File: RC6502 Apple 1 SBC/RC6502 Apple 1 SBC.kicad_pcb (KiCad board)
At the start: 2 copper layers, 99.1 x 99.7 mm, 44 parts, among them J1 VP GND, J2 Arduino Nano, J3 Backplane, J4 Hole, J5 Hole, J6 Hole, J7 Hole, J8 Power, SW1 RESET, U1 WD65C02, U2 HM62256BLP-7, U3 74HCT138, U4 28C256, U5 74HCT00, U6 NE555, U7 74HCT04, U8 WD65C21, U9 MCP23S17, X1 1MHz

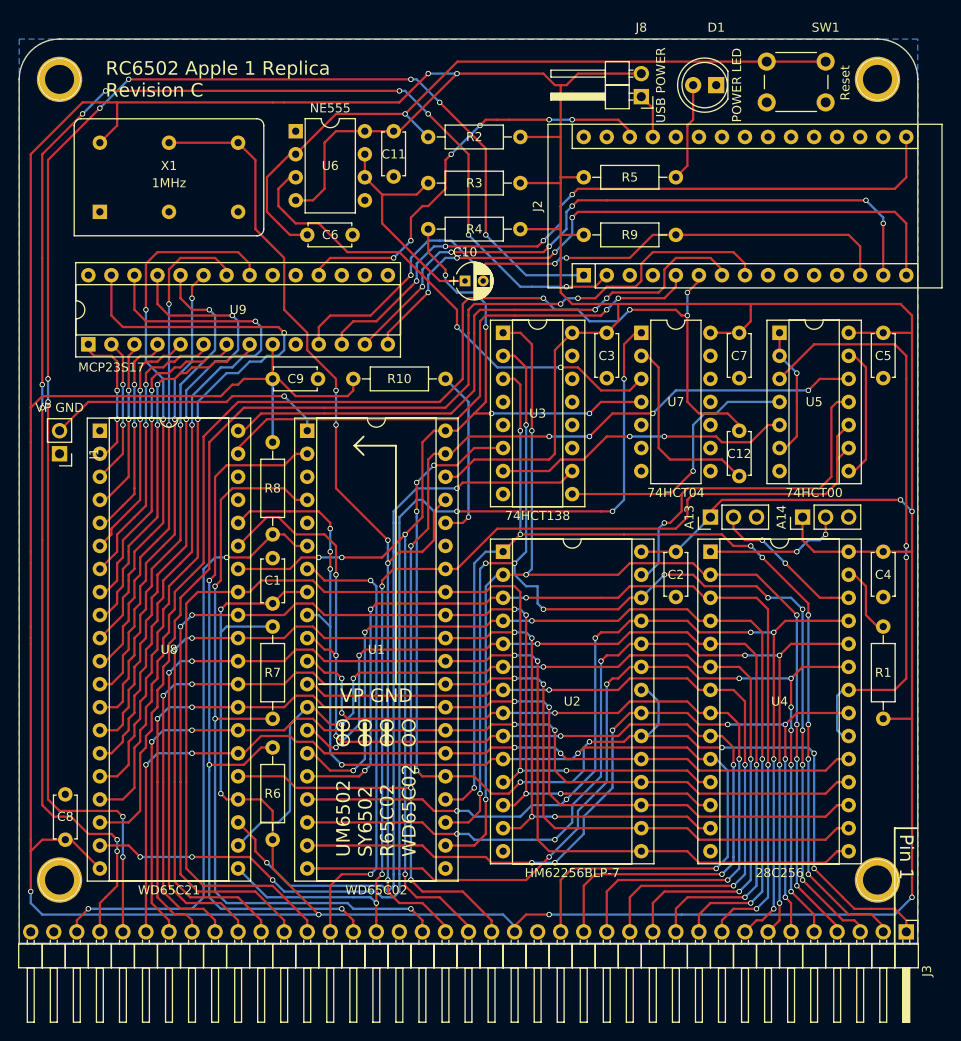
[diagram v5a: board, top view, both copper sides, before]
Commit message: Added resistor values to SBC silkscreen
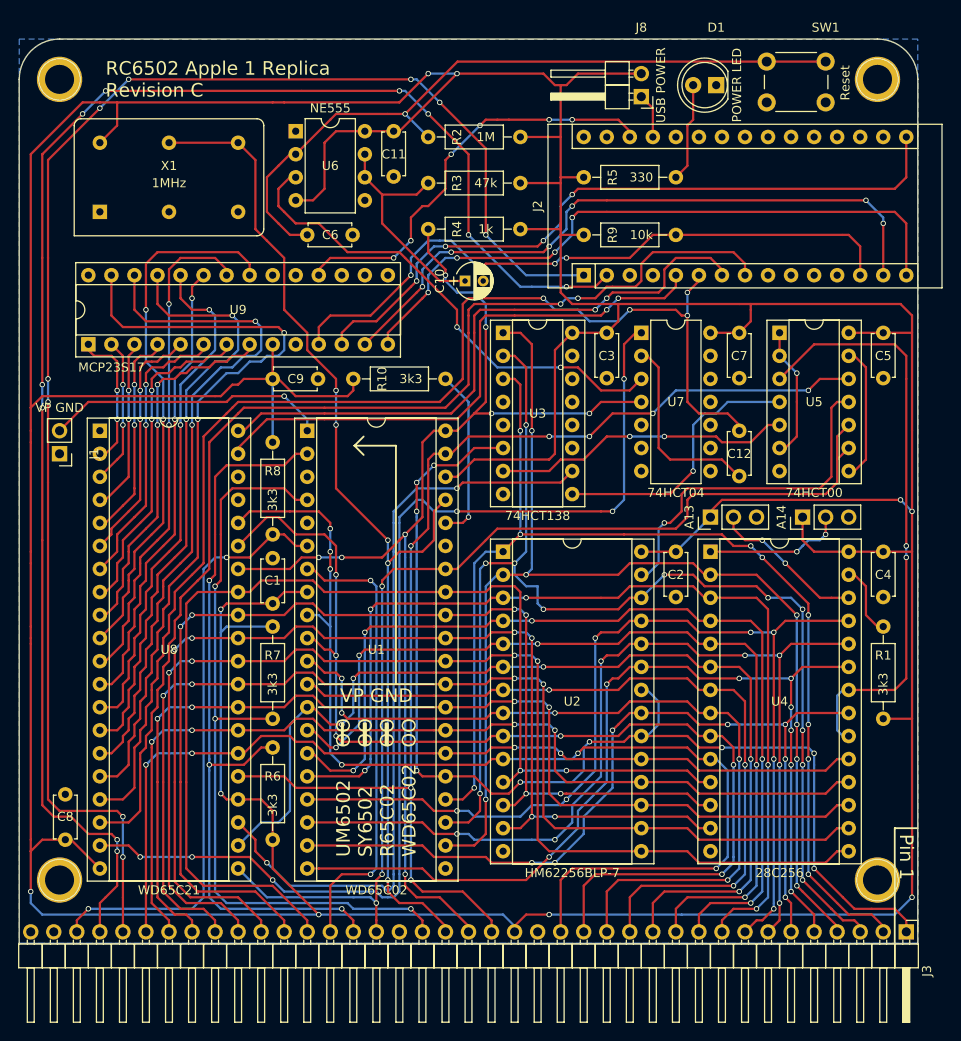
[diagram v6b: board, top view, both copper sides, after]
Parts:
- R1, R10, R6, R7, R8: value 3.3k -> 3k3
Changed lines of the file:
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@@
     (descr "Resistor, Axial_DIN0207 series, Axial, Horizontal, pin pitch=10.16mm, 0.25W = 1/4W, length*diameter=6.3*2.5mm^2, http://cdn-reichelt.de/documents/datenblatt/B400/1_4W%23YAG.pdf")
     (tags "Resistor Axial_DIN0207 series Axial Horizontal pin pitch 10.16mm 0.25W = 1/4W length 6.3mm diameter 2.5mm")
-    (fp_text reference R1 (at 5.08 0 360) (layer F.SilkS)
-      (effects (font (size 1 1) (thickness 0.15)))
-    )
-    (fp_text value 3.3k (at 5.715 -5.08 270) (layer F.Fab)
+    (fp_text reference R1 (at 3.175 0 360) (layer F.SilkS)
+      (effects (font (size 1 1) (thickness 0.15)))
+    )
+    (fp_text value 3k3 (at 6.35 0 270) (layer F.SilkS)
       (effects (font (size 1 1) (thickness 0.15)))
     )
@@
     (descr "Resistor, Axial_DIN0207 series, Axial, Horizontal, pin pitch=10.16mm, 0.25W = 1/4W, length*diameter=6.3*2.5mm^2, http://cdn-reichelt.de/documents/datenblatt/B400/1_4W%23YAG.pdf")
     (tags "Resistor Axial_DIN0207 series Axial Horizontal pin pitch 10.16mm 0.25W = 1/4W length 6.3mm diameter 2.5mm")
-    (fp_text reference R2 (at 5.08 0 180) (layer F.SilkS)
-      (effects (font (size 1 1) (thickness 0.15)))
-    )
-    (fp_text value 1M (at 5.08 1.905 180) (layer F.Fab)
+    (fp_text reference R2 (at 6.985 0 270) (layer F.SilkS)
+      (effects (font (size 1 1) (thickness 0.15)))
+    )
+    (fp_text value 1M (at 3.81 0 180) (layer F.SilkS)
       (effects (font (size 1 1) (thickness 0.15)))
     )
@@
     (descr "Resistor, Axial_DIN0207 series, Axial, Horizontal, pin pitch=10.16mm, 0.25W = 1/4W, length*diameter=6.3*2.5mm^2, http://cdn-reichelt.de/documents/datenblatt/B400/1_4W%23YAG.pdf")
     (tags "Resistor Axial_DIN0207 series Axial Horizontal pin pitch 10.16mm 0.25W = 1/4W length 6.3mm diameter 2.5mm")
-    (fp_text reference R3 (at 5.08 0 180) (layer F.SilkS)
-      (effects (font (size 1 1) (thickness 0.15)))
-    )
-    (fp_text value 47k (at 5.08 1.905 180) (layer F.Fab)
+    (fp_text reference R3 (at 6.985 0 270) (layer F.SilkS)
+      (effects (font (size 1 1) (thickness 0.15)))
+    )
+    (fp_text value 47k (at 3.81 0 180) (layer F.SilkS)
       (effects (font (size 1 1) (thickness 0.15)))
     )
@@
     (descr "Resistor, Axial_DIN0207 series, Axial, Horizontal, pin pitch=10.16mm, 0.25W = 1/4W, length*diameter=6.3*2.5mm^2, http://cdn-reichelt.de/documents/datenblatt/B400/1_4W%23YAG.pdf")
     (tags "Resistor Axial_DIN0207 series Axial Horizontal pin pitch 10.16mm 0.25W = 1/4W length 6.3mm diameter 2.5mm")
-    (fp_text reference R4 (at 5.08 0) (layer F.SilkS)
-      (effects (font (size 1 1) (thickness 0.15)))
-    )
-    (fp_text value 1k (at 5.08 -1.905) (layer F.Fab)
+    (fp_text reference R4 (at 3.175 0 90) (layer F.SilkS)
+      (effects (font (size 1 1) (thickness 0.15)))
+    )
+    (fp_text value 1k (at 6.35 0) (layer F.SilkS)
       (effects (font (size 1 1) (thickness 0.15)))
     )
@@
     (descr "Resistor, Axial_DIN0207 series, Axial, Horizontal, pin pitch=10.16mm, 0.25W = 1/4W, length*diameter=6.3*2.5mm^2, http://cdn-reichelt.de/documents/datenblatt/B400/1_4W%23YAG.pdf")
     (tags "Resistor Axial_DIN0207 series Axial Horizontal pin pitch 10.16mm 0.25W = 1/4W length 6.3mm diameter 2.5mm")
-    (fp_text reference R5 (at 5.08 0) (layer F.SilkS)
-      (effects (font (size 1 1) (thickness 0.15)))
-    )
-    (fp_text value 330 (at 5.08 2.31) (layer F.Fab)
+    (fp_text reference R5 (at 3.175 0 90) (layer F.SilkS)
+      (effects (font (size 1 1) (thickness 0.15)))
+    )
+    (fp_text value 330 (at 6.35 0) (layer F.SilkS)
       (effects (font (size 1 1) (thickness 0.15)))
     )
@@
     (descr "Resistor, Axial_DIN0207 series, Axial, Horizontal, pin pitch=10.16mm, 0.25W = 1/4W, length*diameter=6.3*2.5mm^2, http://cdn-reichelt.de/documents/datenblatt/B400/1_4W%23YAG.pdf")
     (tags "Resistor Axial_DIN0207 series Axial Horizontal pin pitch 10.16mm 0.25W = 1/4W length 6.3mm diameter 2.5mm")
-    (fp_text reference R6 (at 5.08 0 360) (layer F.SilkS)
-      (effects (font (size 1 1) (thickness 0.15)))
-    )
-    (fp_text value 3.3k (at 5.08 4.445 270) (layer F.Fab)
+    (fp_text reference R6 (at 3.175 0 360) (layer F.SilkS)
+      (effects (font (size 1 1) (thickness 0.15)))
+    )
+    (fp_text value 3k3 (at 6.35 0 270) (layer F.SilkS)
       (effects (font (size 1 1) (thickness 0.15)))
     )
@@
     (descr "Resistor, Axial_DIN0207 series, Axial, Horizontal, pin pitch=10.16mm, 0.25W = 1/4W, length*diameter=6.3*2.5mm^2, http://cdn-reichelt.de/documents/datenblatt/B400/1_4W%23YAG.pdf")
     (tags "Resistor Axial_DIN0207 series Axial Horizontal pin pitch 10.16mm 0.25W = 1/4W length 6.3mm diameter 2.5mm")
-    (fp_text reference R7 (at 5.08 0 180) (layer F.SilkS)
-      (effects (font (size 1 1) (thickness 0.15)))
-    )
-    (fp_text value 3.3k (at 5.08 -4.445 90) (layer F.Fab)
+    (fp_text reference R7 (at 6.985 0 180) (layer F.SilkS)
+      (effects (font (size 1 1) (thickness 0.15)))
+    )
+    (fp_text value 3k3 (at 3.81 0 90) (layer F.SilkS)
       (effects (font (size 1 1) (thickness 0.15)))
     )
@@
     (descr "Resistor, Axial_DIN0207 series, Axial, Horizontal, pin pitch=10.16mm, 0.25W = 1/4W, length*diameter=6.3*2.5mm^2, http://cdn-reichelt.de/documents/datenblatt/B400/1_4W%23YAG.pdf")
     (tags "Resistor Axial_DIN0207 series Axial Horizontal pin pitch 10.16mm 0.25W = 1/4W length 6.3mm diameter 2.5mm")
-    (fp_text reference R8 (at 5.08 0 180) (layer F.SilkS)
-      (effects (font (size 1 1) (thickness 0.15)))
-    )
-    (fp_text value 3.3k (at 5.08 -4.445 90) (layer F.Fab)
+    (fp_text reference R8 (at 6.985 0 180) (layer F.SilkS)
+      (effects (font (size 1 1) (thickness 0.15)))
+    )
+    (fp_text value 3k3 (at 3.81 0 90) (layer F.SilkS)
       (effects (font (size 1 1) (thickness 0.15)))
     )
@@
     (descr "Resistor, Axial_DIN0207 series, Axial, Horizontal, pin pitch=10.16mm, 0.25W = 1/4W, length*diameter=6.3*2.5mm^2, http://cdn-reichelt.de/documents/datenblatt/B400/1_4W%23YAG.pdf")
     (tags "Resistor Axial_DIN0207 series Axial Horizontal pin pitch 10.16mm 0.25W = 1/4W length 6.3mm diameter 2.5mm")
-    (fp_text reference R9 (at 5.08 0) (layer F.SilkS)
-      (effects (font (size 1 1) (thickness 0.15)))
-    )
-    (fp_text value 10k (at 5.08 2.31) (layer F.Fab)
+    (fp_text reference R9 (at 3.175 0 90) (layer F.SilkS)
+      (effects (font (size 1 1) (thickness 0.15)))
+    )
+    (fp_text value 10k (at 6.35 0) (layer F.SilkS)
       (effects (font (size 1 1) (thickness 0.15)))
     )
@@
     (descr "CP, Radial series, Radial, pin pitch=2.00mm, , diameter=4mm, Electrolytic Capacitor")
     (tags "CP Radial series Radial pin pitch 2.00mm  diameter 4mm Electrolytic Capacitor")
-    (fp_text reference C10 (at 0 -3.175) (layer F.SilkS)
+    (fp_text reference C10 (at -2.794 0 90) (layer F.SilkS)
       (effects (font (size 1 1) (thickness 0.15)))
     )
@@
       (effects (font (size 1 1) (thickness 0.15)))
     )
-    (fp_text user %R (at 0 -3.175) (layer F.Fab)
+    (fp_text user %R (at -2.794 0 90) (layer F.Fab)
       (effects (font (size 1 1) (thickness 0.15)))
     )
@@
     (descr "Resistor, Axial_DIN0207 series, Axial, Horizontal, pin pitch=10.16mm, 0.25W = 1/4W, length*diameter=6.3*2.5mm^2, http://cdn-reichelt.de/documents/datenblatt/B400/1_4W%23YAG.pdf")
     (tags "Resistor Axial_DIN0207 series Axial Horizontal pin pitch 10.16mm 0.25W = 1/4W length 6.3mm diameter 2.5mm")
-    (fp_text reference R10 (at 5.08 0 180) (layer F.SilkS)
-      (effects (font (size 1 1) (thickness 0.15)))
-    )
-    (fp_text value 3.3k (at 5.08 2.31 180) (layer F.Fab)
+    (fp_text reference R10 (at 6.985 0 270) (layer F.SilkS)
+      (effects (font (size 1 1) (thickness 0.15)))
+    )
+    (fp_text value 3k3 (at 3.81 0 180) (layer F.SilkS)
       (effects (font (size 1 1) (thickness 0.15)))
     )
@@
   (via (at 158.75 93.98) (size 0.6) (drill 0.4) (layers F.Cu B.Cu) (net 33))
   (segment (start 165.735 137.795) (end 165.735 137.16) (width 0.25) (layer F.Cu) (net 33))
-  (segment (start 132.715 50.8) (end 140.335 50.8) (width 0.25) (layer F.Cu) (net 34) (status C00000))
+  (segment (start 132.715 50.8) (end 140.335 50.8) (width 0.25) (layer F.Cu) (net 34))
   (segment (start 143.51 61.595) (end 142.24 60.325) (width 0.25) (layer F.Cu) (net 34))
   (via (at 151.13 78.105) (size 0.6) (drill 0.4) (layers F.Cu B.Cu) (net 34))

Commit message: Added ROM enable jumper to SBC
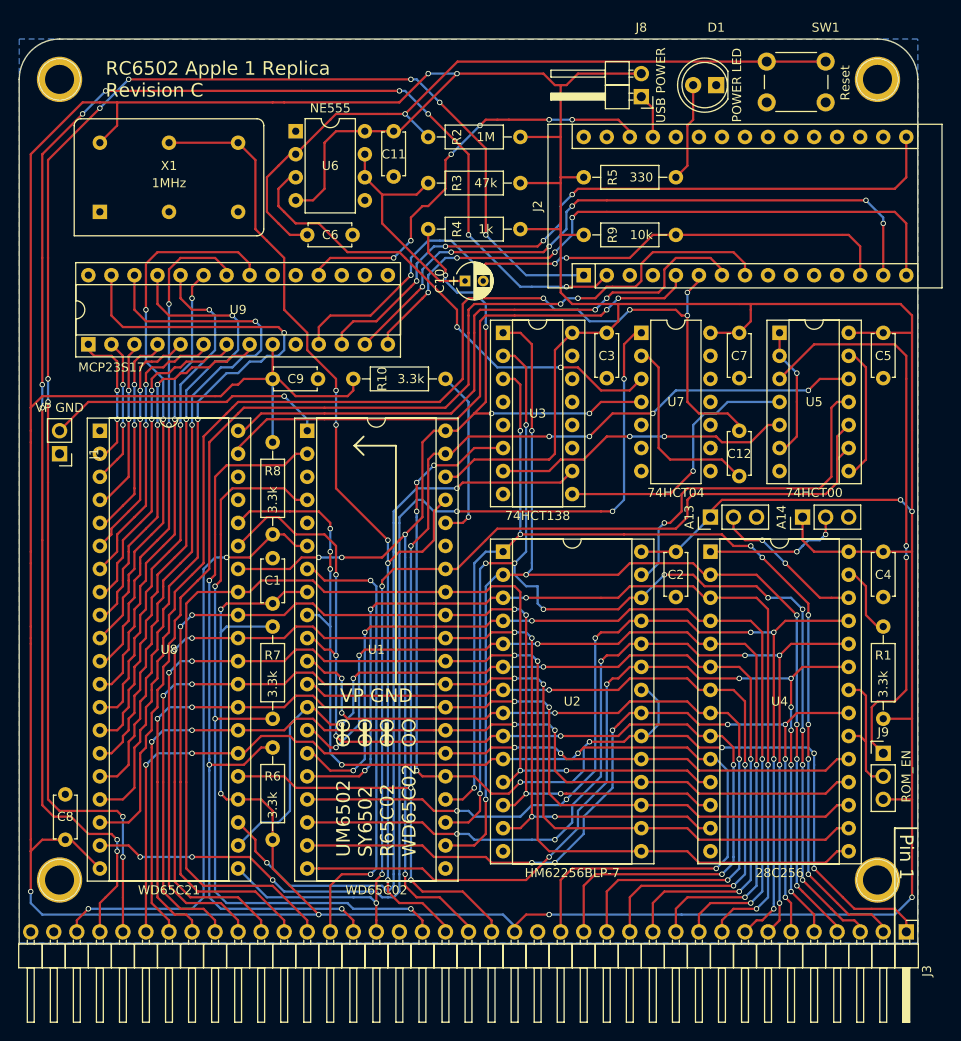
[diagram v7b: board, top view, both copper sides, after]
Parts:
- added J9: ROM_EN, Pin_Headers:Pin_Header_Straight_1x03_Pitch2.54mm, F.Cu at (211.5, 118.1)
- R1, R10, R6, R7, R8: value 3k3 -> 3.3k
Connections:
- U4 pad 20: CS_ROM -> Net-(J9-Pad2)
- U4 pad 22: CS_ROM -> Net-(J9-Pad2)
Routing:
- net Net-(J9-Pad2): track 0.00 -> 14.8 mm
- net VCC: track 648.5 -> 651.7 mm
- net CS_ROM: track 65.4 -> 63.1 mm
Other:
- board text added: "ROM_EN"

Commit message: Added RAM enable jumper to SBC
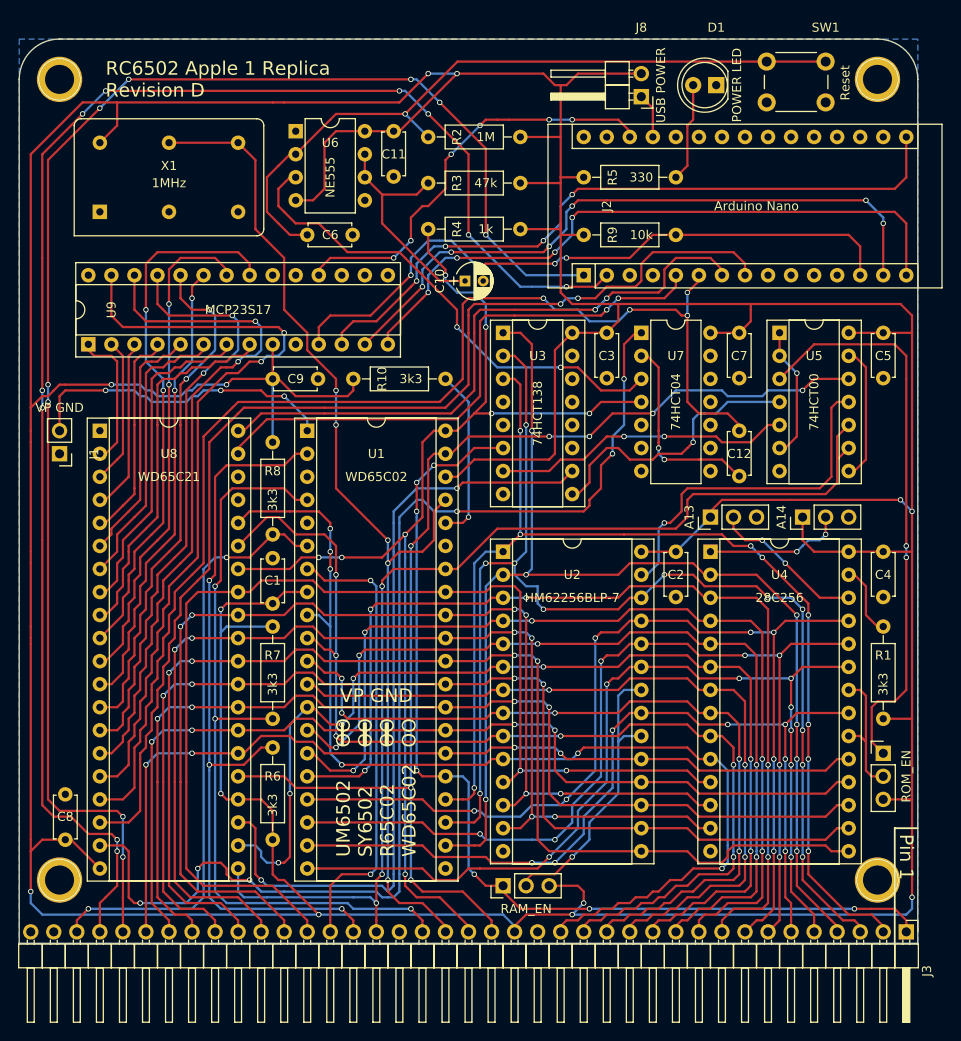
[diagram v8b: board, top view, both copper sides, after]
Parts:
- added J10: RAM_EN, Pin_Headers:Pin_Header_Straight_1x03_Pitch2.54mm, F.Cu at (169.5, 132.7)
- R1, R10, R6, R7, R8: value 3.3k -> 3k3
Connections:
- U2 pad 20: A15 -> Net-(J10-Pad2)
- U2 pad 22: A15 -> Net-(J10-Pad2)
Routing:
- net Net-(J10-Pad2): track 0.00 -> 32.3 mm, vias 0 -> 1
- net A15: track 126.5 -> 110.9 mm, vias 9 -> 7
- net VCC: track 651.7 -> 661.0 mm, vias 10 -> 13
- net Net-(U7-Pad1): track 123.1 -> 129.8 mm
- net A4: track 112.9 -> 116.7 mm, vias 5 -> 7
- net Net-(J1-Pad2): track 31.2 -> 35.0 mm, vias 1 -> 3
- net A0: track 120.6 -> 118.0 mm
- net CS_PIA: track 84.1 -> 86.3 mm
- net A1: track 119.6 -> 117.4 mm
- net A2: track 90.3 -> 88.4 mm
- net A3: track 87.2 -> 85.8 mm
- net RW: track 120.9 -> 122.4 mm
- net D3: track 132.3 -> 133.2 mm
- net A5: track 99.0 -> 98.2 mm
- net Net-(U3-Pad9): track 30.0 -> 30.7 mm
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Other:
- board text added: "RAM_EN"
- board text added: "RC6502 Apple 1 Replica Revision D"
- board text added: "https://hvetebolle.blogspot.com"
- board text removed: "Backplane Connector"
- board text removed: "RC6502 Apple 1 Replica Revision C"
